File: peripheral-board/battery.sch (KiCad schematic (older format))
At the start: 19 parts

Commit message: added audio jack
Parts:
- U5002, U5003: renamed from U?; footprint (none) -> TO_SOT_Packages_SMD:SOT-23
- gave numbers to parts that had none: 17
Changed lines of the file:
@@
 $EndDescr
 $Comp
-L Battery_Cell BT?
+L Battery_Cell BT5001
 U 1 1 589ABFFA
 P 7000 2800
-F 0 "BT?" H 7118 2896 50  0000 L CNN
+F 0 "BT5001" H 7118 2896 50  0000 L CNN
 F 1 "LiPo" H 7118 2805 50  0000 L CNN
 F 2 "" V -3000 810 50  0001 C CNN
@@
 $EndComp
 $Comp
-L TL431 U?
+L TL431 U5002
 U 1 1 589AC001
 P 5550 2800
-F 0 "U?" H 5677 2853 60  0000 L CNN
+F 0 "U5002" H 5677 2853 60  0000 L CNN
 F 1 "TL431" H 5677 2747 60  0000 L CNN
-F 2 "" H -4350 1000 60  0001 C CNN
+F 2 "TO_SOT_Packages_SMD:SOT-23" H -4350 1000 60  0001 C CNN
 F 3 "" H -4350 1000 60  0001 C CNN
 	1    5550 2800
@@
 $EndComp
 $Comp
-L POT RV?
+L POT RV5001
 U 1 1 589AC008
 P 5000 2800
-F 0 "RV?" H 4930 2846 50  0000 R CNN
+F 0 "RV5001" H 4930 2846 50  0000 R CNN
 F 1 "47k" H 4930 2755 50  0000 R CNN
 F 2 "" H -4200 1800 50  0001 C CNN
@@
 $EndComp
 $Comp
-L R R?
+L R R5002
 U 1 1 589AC00F
 P 5000 2500
-F 0 "R?" H 5070 2546 50  0000 L CNN
+F 0 "R5002" H 5070 2546 50  0000 L CNN
 F 1 "150k" H 5070 2455 50  0000 L CNN
 F 2 "" V -3770 1300 50  0001 C CNN
@@
 $EndComp
 $Comp
-L R R?
+L R R5005
 U 1 1 589AC016
 P 5000 3100
-F 0 "R?" H 5070 3146 50  0000 L CNN
+F 0 "R5005" H 5070 3146 50  0000 L CNN
 F 1 "220k" H 5070 3055 50  0000 L CNN
 F 2 "" V -3720 650 50  0001 C CNN
@@
 $EndComp
 $Comp
-L R R?
+L R R5001
 U 1 1 589AC01D
 P 5550 2300
-F 0 "R?" H 5620 2346 50  0000 L CNN
+F 0 "R5001" H 5620 2346 50  0000 L CNN
 F 1 "10k" H 5620 2255 50  0000 L CNN
 F 2 "" V -3720 1100 50  0001 C CNN
@@
 $EndComp
 $Comp
-L R R?
+L R R5003
 U 1 1 589AC024
 P 6100 2900
-F 0 "R?" H 6170 2946 50  0000 L CNN
+F 0 "R5003" H 6170 2946 50  0000 L CNN
 F 1 "40R" H 6170 2855 50  0000 L CNN
 F 2 "" V -3870 800 50  0001 C CNN
@@
 Connection ~ 5550 3300
 $Comp
-L Battery_Cell BT?
+L Battery_Cell BT5002
 U 1 1 589AC03D
 P 7000 3950
-F 0 "BT?" H 7118 4046 50  0000 L CNN
+F 0 "BT5002" H 7118 4046 50  0000 L CNN
 F 1 "LiPo" H 7118 3955 50  0000 L CNN
 F 2 "" V -3000 1960 50  0001 C CNN
@@
 $EndComp
 $Comp
-L TL431 U?
+L TL431 U5003
 U 1 1 589AC044
 P 5550 3950
-F 0 "U?" H 5677 4003 60  0000 L CNN
+F 0 "U5003" H 5677 4003 60  0000 L CNN
 F 1 "TL431" H 5677 3897 60  0000 L CNN
-F 2 "" H -4350 2150 60  0001 C CNN
+F 2 "TO_SOT_Packages_SMD:SOT-23" H -4350 2150 60  0001 C CNN
 F 3 "" H -4350 2150 60  0001 C CNN
 	1    5550 3950
@@
 $EndComp
 $Comp
-L POT RV?
+L POT RV5002
 U 1 1 589AC04B
 P 5000 3950
-F 0 "RV?" H 4930 3996 50  0000 R CNN
+F 0 "RV5002" H 4930 3996 50  0000 R CNN
 F 1 "47k" H 4930 3905 50  0000 R CNN
 F 2 "" H -4200 2950 50  0001 C CNN
@@
 $EndComp
 $Comp
-L R R?
+L R R5007
 U 1 1 589AC052
 P 5000 3650
-F 0 "R?" H 5070 3696 50  0000 L CNN
+F 0 "R5007" H 5070 3696 50  0000 L CNN
 F 1 "150k" H 5070 3605 50  0000 L CNN
 F 2 "" V -3770 2450 50  0001 C CNN
@@
 $EndComp
 $Comp
-L R R?
+L R R5010
 U 1 1 589AC059
 P 5000 4250
-F 0 "R?" H 5070 4296 50  0000 L CNN
+F 0 "R5010" H 5070 4296 50  0000 L CNN
 F 1 "220k" H 5070 4205 50  0000 L CNN
 F 2 "" V -3720 1800 50  0001 C CNN
@@
 $EndComp
 $Comp
-L R R?
+L R R5006
 U 1 1 589AC060
 P 5550 3450
-F 0 "R?" H 5620 3496 50  0000 L CNN
+F 0 "R5006" H 5620 3496 50  0000 L CNN
 F 1 "10k" H 5620 3405 50  0000 L CNN
 F 2 "" V -3720 2250 50  0001 C CNN
@@
 $EndComp
 $Comp
-L R R?
+L R R5008
 U 1 1 589AC067
 P 6100 4050
-F 0 "R?" H 6170 4096 50  0000 L CNN
+F 0 "R5008" H 6170 4096 50  0000 L CNN
 F 1 "40R" H 6170 4005 50  0000 L CNN
 F 2 "" V -3870 1950 50  0001 C CNN
@@
 Connection ~ 5550 4450
 $Comp
-L Thermistor_NTC TH?
+L Thermistor_NTC TH5001
 U 1 1 589AC07A
 P 4150 4250
-F 0 "TH?" H 4247 4296 50  0000 L CNN
+F 0 "TH5001" H 4247 4296 50  0000 L CNN
 F 1 "10k" H 4247 4205 50  0000 L CNN
 F 2 "" H -3550 3150 50  0001 C CNN
@@
 $EndComp
 $Comp
-L Q_PMOS_DGS Q?
+L Q_PMOS_DGS Q5001
 U 1 1 589AC081
 P 6000 2500
-F 0 "Q?" H 6206 2454 50  0000 L CNN
+F 0 "Q5001" H 6206 2454 50  0000 L CNN
 F 1 "Q_PMOS_DGS" H 6206 2545 50  0000 L CNN
 F 2 "" H -3400 1600 50  0001 C CNN
@@
 $EndComp
 $Comp
-L Q_PMOS_DGS Q?
+L Q_PMOS_DGS Q5002
 U 1 1 589AC088
 P 6000 3650
-F 0 "Q?" H 6206 3604 50  0000 L CNN
+F 0 "Q5002" H 6206 3604 50  0000 L CNN
 F 1 "Q_PMOS_DGS" H 6206 3695 50  0000 L CNN
 F 2 "" H -3400 2750 50  0001 C CNN
@@
 Connection ~ 7000 3300
 $Comp
-L R R?
+L R R5004
 U 1 1 589AEB2B
 P 6400 2900
-F 0 "R?" H 6470 2946 50  0000 L CNN
+F 0 "R5004" H 6470 2946 50  0000 L CNN
 F 1 "40R" H 6470 2855 50  0000 L CNN
 F 2 "" V -3570 800 50  0001 C CNN
@@
 	6400 3050 6100 3050
 $Comp
-L R R?
+L R R5009
 U 1 1 589AEC5C
 P 6400 4050
-F 0 "R?" H 6470 4096 50  0000 L CNN
+F 0 "R5009" H 6470 4096 50  0000 L CNN
 F 1 "40R" H 6470 4005 50  0000 L CNN
 F 2 "" V -3570 1950 50  0001 C CNN

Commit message: audio circuitry
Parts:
- R5001, R5002, R5003, R5004, R5005, R5006, R5007, R5008, R5009, R5010: footprint (none) -> Resistors_SMD:R_0805
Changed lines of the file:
@@
 EESchema Schematic File Version 2
+LIBS:peripheral-board-rescue
 LIBS:power
 LIBS:device
@@
 LIBS:digital-pot
 LIBS:vref
+LIBS:switches
 LIBS:peripheral-board-cache
 EELAYER 26 0
@@
 F 0 "R5002" H 5070 2546 50  0000 L CNN
 F 1 "150k" H 5070 2455 50  0000 L CNN
-F 2 "" V -3770 1300 50  0001 C CNN
+F 2 "Resistors_SMD:R_0805" V -3770 1300 50  0001 C CNN
 F 3 "" H -3700 1300 50  0001 C CNN
 	1    5000 2500
@@
 F 0 "R5005" H 5070 3146 50  0000 L CNN
 F 1 "220k" H 5070 3055 50  0000 L CNN
-F 2 "" V -3720 650 50  0001 C CNN
+F 2 "Resistors_SMD:R_0805" V -3720 650 50  0001 C CNN
 F 3 "" H -3650 650 50  0001 C CNN
 	1    5000 3100
@@
 F 0 "R5001" H 5620 2346 50  0000 L CNN
 F 1 "10k" H 5620 2255 50  0000 L CNN
-F 2 "" V -3720 1100 50  0001 C CNN
+F 2 "Resistors_SMD:R_0805" V -3720 1100 50  0001 C CNN
 F 3 "" H -3650 1100 50  0001 C CNN
 	1    5550 2300
@@
 F 0 "R5003" H 6170 2946 50  0000 L CNN
 F 1 "40R" H 6170 2855 50  0000 L CNN
-F 2 "" V -3870 800 50  0001 C CNN
+F 2 "Resistors_SMD:R_0805" V -3870 800 50  0001 C CNN
 F 3 "" H -3800 800 50  0001 C CNN
 	1    6100 2900
@@
 F 0 "R5007" H 5070 3696 50  0000 L CNN
 F 1 "150k" H 5070 3605 50  0000 L CNN
-F 2 "" V -3770 2450 50  0001 C CNN
+F 2 "Resistors_SMD:R_0805" V -3770 2450 50  0001 C CNN
 F 3 "" H -3700 2450 50  0001 C CNN
 	1    5000 3650
@@
 F 0 "R5010" H 5070 4296 50  0000 L CNN
 F 1 "220k" H 5070 4205 50  0000 L CNN
-F 2 "" V -3720 1800 50  0001 C CNN
+F 2 "Resistors_SMD:R_0805" V -3720 1800 50  0001 C CNN
 F 3 "" H -3650 1800 50  0001 C CNN
 	1    5000 4250
@@
 F 0 "R5006" H 5620 3496 50  0000 L CNN
 F 1 "10k" H 5620 3405 50  0000 L CNN
-F 2 "" V -3720 2250 50  0001 C CNN
+F 2 "Resistors_SMD:R_0805" V -3720 2250 50  0001 C CNN
 F 3 "" H -3650 2250 50  0001 C CNN
 	1    5550 3450
@@
 F 0 "R5008" H 6170 4096 50  0000 L CNN
 F 1 "40R" H 6170 4005 50  0000 L CNN
-F 2 "" V -3870 1950 50  0001 C CNN
+F 2 "Resistors_SMD:R_0805" V -3870 1950 50  0001 C CNN
 F 3 "" H -3800 1950 50  0001 C CNN
 	1    6100 4050
@@
 F 0 "R5004" H 6470 2946 50  0000 L CNN
 F 1 "40R" H 6470 2855 50  0000 L CNN
-F 2 "" V -3570 800 50  0001 C CNN
+F 2 "Resistors_SMD:R_0805" V -3570 800 50  0001 C CNN
 F 3 "" H -3500 800 50  0001 C CNN
 	1    6400 2900
@@
 F 0 "R5009" H 6470 4096 50  0000 L CNN
 F 1 "40R" H 6470 4005 50  0000 L CNN
-F 2 "" V -3570 1950 50  0001 C CNN
+F 2 "Resistors_SMD:R_0805" V -3570 1950 50  0001 C CNN
 F 3 "" H -3500 1950 50  0001 C CNN
 	1    6400 4050

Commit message: power supply component placement
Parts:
- removed Q5001, Q5002: Q_PMOS_DGS, symbol Q_PMOS_DGS
- added Q5001, Q5002: IRLML2244TRPbF, TO_SOT_Packages_SMD:SOT-23, symbol Q_PMOS_GSD
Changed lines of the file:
@@
 	1    0    0    -1
-$EndComp
-$Comp
-L Q_PMOS_DGS Q5001
-U 1 1 589AC081
-P 6000 2500
-F 0 "Q5001" H 6206 2454 50  0000 L CNN
-F 1 "Q_PMOS_DGS" H 6206 2545 50  0000 L CNN
-F 2 "" H -3400 1600 50  0001 C CNN
-F 3 "" H -3600 1500 50  0001 C CNN
-	1    6000 2500
-	1    0    0    1
-$EndComp
-$Comp
-L Q_PMOS_DGS Q5002
-U 1 1 589AC088
-P 6000 3650
-F 0 "Q5002" H 6206 3604 50  0000 L CNN
-F 1 "Q_PMOS_DGS" H 6206 3695 50  0000 L CNN
-F 2 "" H -3400 2750 50  0001 C CNN
-F 3 "" H -3600 2650 50  0001 C CNN
-	1    6000 3650
-	1    0    0    1
 $EndComp
 Text HLabel 3350 2150 0    60   UnSpc ~ 0
@@
 Text Notes 6150 4300 0    60   ~ 0
 2 × 1/4 W
+$Comp
+L Q_PMOS_GSD Q5001
+U 1 1 58A97AA9
+P 6000 2500
+F 0 "Q5001" H 6206 2454 50  0000 L CNN
+F 1 "IRLML2244TRPbF" H 6206 2545 50  0000 L CNN
+F 2 "TO_SOT_Packages_SMD:SOT-23" H -850 700 50  0001 C CNN
+F 3 "" H -1050 600 50  0001 C CNN
+	1    6000 2500
+	1    0    0    1
+$EndComp
+$Comp
+L Q_PMOS_GSD Q5002
+U 1 1 58A97BDE
+P 6000 3650
+F 0 "Q5002" H 6206 3604 50  0000 L CNN
+F 1 "IRLML2244TRPbF" H 6206 3695 50  0000 L CNN
+F 2 "TO_SOT_Packages_SMD:SOT-23" H -850 1850 50  0001 C CNN
+F 3 "" H -1050 1750 50  0001 C CNN
+	1    6000 3650
+	1    0    0    1
+$EndComp
 $EndSCHEMATC

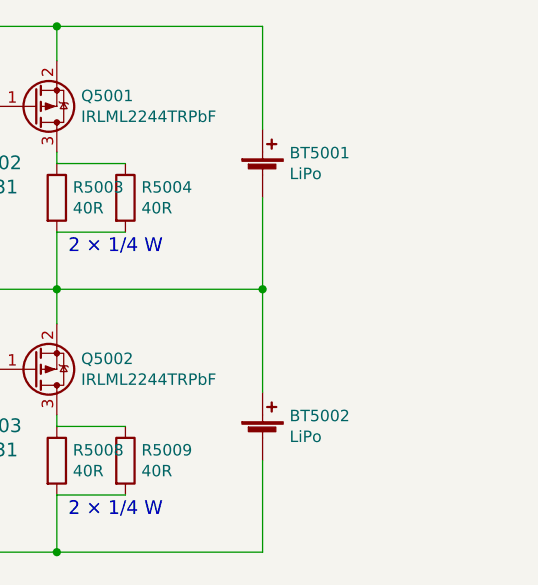
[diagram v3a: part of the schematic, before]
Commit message: audio components placement
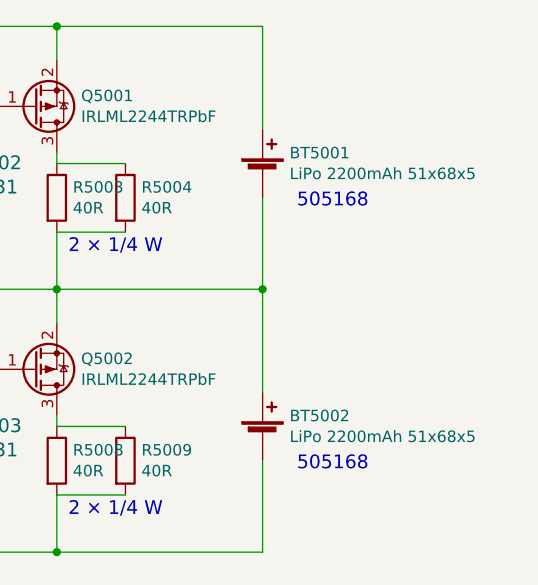
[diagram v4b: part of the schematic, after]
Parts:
- BT5001, BT5002: value LiPo -> LiPo 2200mAh 51x68x5
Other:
- note added: "505168"
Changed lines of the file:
@@
 P 7000 2800
 F 0 "BT5001" H 7118 2896 50  0000 L CNN
-F 1 "LiPo" H 7118 2805 50  0000 L CNN
+F 1 "LiPo 2200mAh 51x68x5" H 7118 2805 50  0000 L CNN
 F 2 "" V -3000 810 50  0001 C CNN
 F 3 "" V -3000 810 50  0001 C CNN
@@
 P 7000 3950
 F 0 "BT5002" H 7118 4046 50  0000 L CNN
-F 1 "LiPo" H 7118 3955 50  0000 L CNN
+F 1 "LiPo 2200mAh 51x68x5" H 7118 3955 50  0000 L CNN
 F 2 "" V -3000 1960 50  0001 C CNN
 F 3 "" V -3000 1960 50  0001 C CNN
@@
 	1    0    0    1
 $EndComp
+Text Notes 7150 2950 0    60   ~ 0
+505168
+Text Notes 7150 4100 0    60   ~ 0
+505168
 $EndSCHEMATC

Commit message: routed traces.
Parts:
- TH5001: footprint (none) -> Capacitors_ThroughHole:CP_Radial_Tantal_D4.5mm_P2.50mm
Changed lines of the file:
@@
 F 0 "TH5001" H 4247 4296 50  0000 L CNN
 F 1 "10k" H 4247 4205 50  0000 L CNN
-F 2 "" H -3550 3150 50  0001 C CNN
+F 2 "Capacitors_ThroughHole:CP_Radial_Tantal_D4.5mm_P2.50mm" H -3550 3150 50  0001 C CNN
 F 3 "" H -3550 3150 50  0001 C CNN
 	1    4150 4250

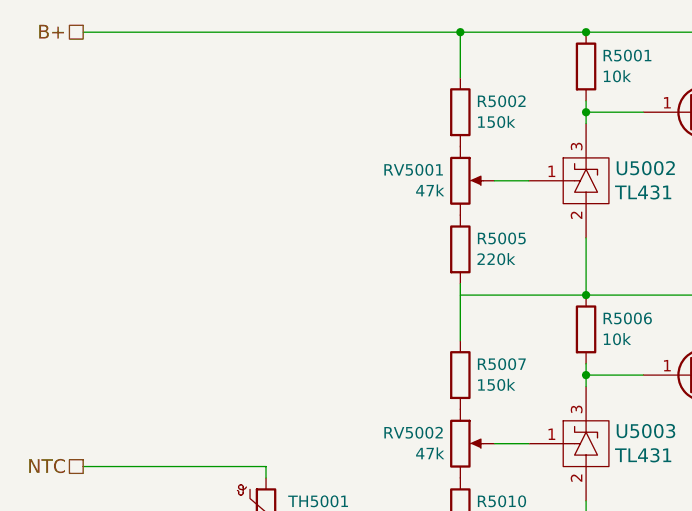
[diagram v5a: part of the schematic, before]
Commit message: misc traces, headphone jack 3d
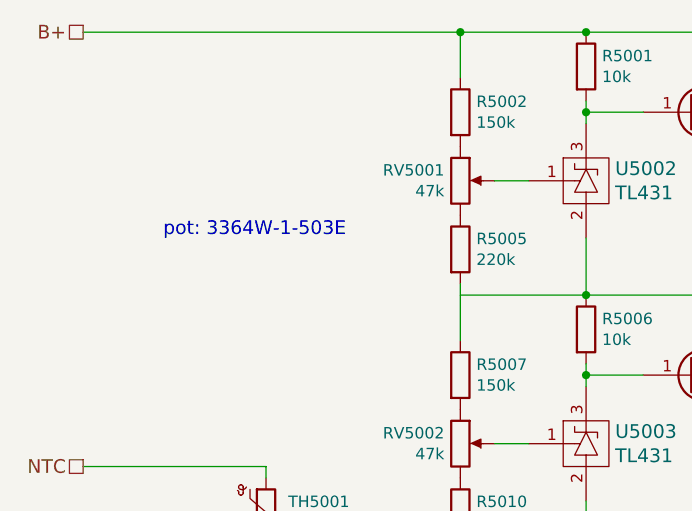
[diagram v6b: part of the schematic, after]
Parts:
- RV5001, RV5002: footprint (none) -> lib:3364W
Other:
- note added: "pot: 3364W-1-503E"
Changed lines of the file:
@@
 F 0 "RV5001" H 4930 2846 50  0000 R CNN
 F 1 "47k" H 4930 2755 50  0000 R CNN
-F 2 "" H -4200 1800 50  0001 C CNN
+F 2 "lib:3364W" H -4200 1800 50  0001 C CNN
 F 3 "" H -4200 1800 50  0001 C CNN
 	1    5000 2800
@@
 F 0 "RV5002" H 4930 3996 50  0000 R CNN
 F 1 "47k" H 4930 3905 50  0000 R CNN
-F 2 "" H -4200 2950 50  0001 C CNN
+F 2 "lib:3364W" H -4200 2950 50  0001 C CNN
 F 3 "" H -4200 2950 50  0001 C CNN
 	1    5000 3950
@@
 Text Notes 7150 4100 0    60   ~ 0
 505168
+Text Notes 3700 3050 0    60   ~ 0
+pot: 3364W-1-503E
 $EndSCHEMATC

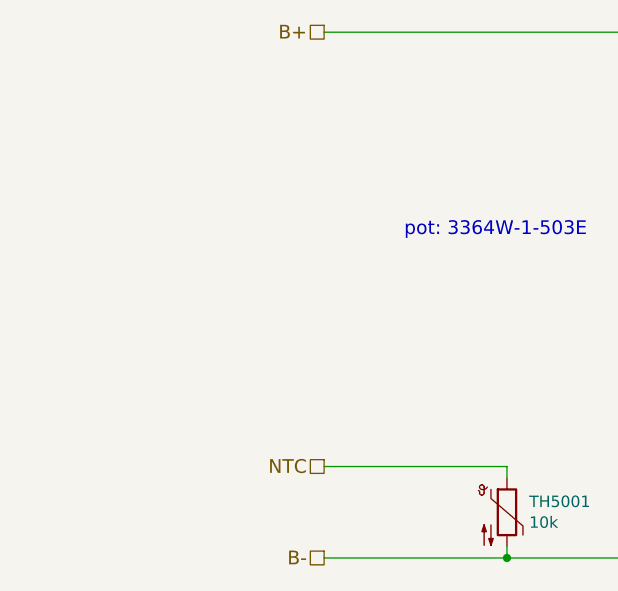
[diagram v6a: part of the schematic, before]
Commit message: added display board
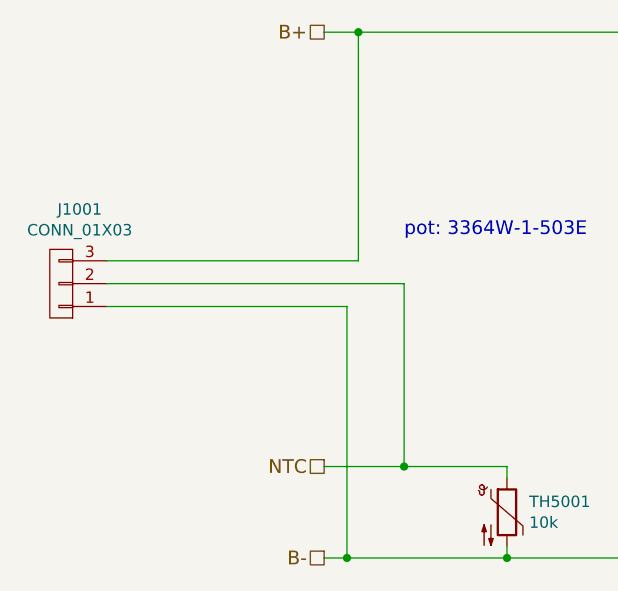
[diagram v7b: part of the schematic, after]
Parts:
- added J1001: CONN_01X03, Socket_Strips:Socket_Strip_Straight_1x03_Pitch2.54mm, symbol CONN_01X03
- BT5001, BT5002: footprint (none) -> Socket_Strips:Socket_Strip_Straight_1x02_Pitch1.27mm
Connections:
- net B+: now also J1001.3 (P3)
- net B-: now also J1001.1 (P1)
- net NTC: now also J1001.2 (P2)
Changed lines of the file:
@@
 EESchema Schematic File Version 2
-LIBS:peripheral-board-rescue
 LIBS:power
 LIBS:device
@@
 LIBS:contrib
 LIBS:valves
-LIBS:amp
-LIBS:card-edge
-LIBS:switchmode
-LIBS:joystick
-LIBS:digital-pot
 LIBS:vref
-LIBS:switches
-LIBS:peripheral-board-cache
+LIBS:battery-cache
 EELAYER 26 0
 EELAYER END
 $Descr A4 11693 8268
 encoding utf-8
-Sheet 5 10
+Sheet 1 1
 Title ""
 Date ""
@@
 F 0 "BT5001" H 7118 2896 50  0000 L CNN
 F 1 "LiPo 2200mAh 51x68x5" H 7118 2805 50  0000 L CNN
-F 2 "" V -3000 810 50  0001 C CNN
+F 2 "Socket_Strips:Socket_Strip_Straight_1x02_Pitch1.27mm" V -3000 810 50  0001 C CNN
 F 3 "" V -3000 810 50  0001 C CNN
 	1    7000 2800
@@
 F 0 "BT5002" H 7118 4046 50  0000 L CNN
 F 1 "LiPo 2200mAh 51x68x5" H 7118 3955 50  0000 L CNN
-F 2 "" V -3000 1960 50  0001 C CNN
+F 2 "Socket_Strips:Socket_Strip_Straight_1x02_Pitch1.27mm" V -3000 1960 50  0001 C CNN
 F 3 "" V -3000 1960 50  0001 C CNN
 	1    7000 3950
@@
 Text Notes 3700 3050 0    60   ~ 0
 pot: 3364W-1-503E
+$Comp
+L CONN_01X03 J1001
+U 1 1 58E61493
+P 2200 3250
+F 0 "J1001" H 2119 2925 50  0000 C CNN
+F 1 "CONN_01X03" H 2119 3016 50  0000 C CNN
+F 2 "Socket_Strips:Socket_Strip_Straight_1x03_Pitch2.54mm" H 2200 3250 50  0001 C CNN
+F 3 "" H 2200 3250 50  0001 C CNN
+	1    2200 3250
+	-1   0    0    1
+$EndComp
+Wire Wire Line
+	2400 3150 3500 3150
+Wire Wire Line
+	3500 3150 3500 2150
+Connection ~ 3500 2150
+Wire Wire Line
+	2400 3250 3700 3250
+Wire Wire Line
+	3700 3250 3700 4050
+Connection ~ 3700 4050
+Wire Wire Line
+	2400 3350 3450 3350
+Wire Wire Line
+	3450 3350 3450 4450
+Connection ~ 3450 4450
 $EndSCHEMATC

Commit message: fixed faulty schematic in battery balancer
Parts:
- U5002, U5003: symbol TL431 -> TL431DBZ
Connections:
- net B-: now also U5003.3 (A); no longer U5003.2
- net at BT5001.2 (-), BT5002.1 (+), Q5002.2 (S)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: now also R5005.2, R5007.1, U5002.3 (A); no longer U5002.2
- net at U5002.1 (K): now also Q5001.1 (G), R5001.2; no longer RV5001.2
- net at U5003.1 (K): now also Q5002.1 (G), R5006.2; no longer RV5002.2
- new net: RV5001.2, U5002.2 (REF)
- new net: RV5002.2, U5003.2 (REF)
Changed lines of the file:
@@
 LIBS:valves
 LIBS:vref
+LIBS:references
 LIBS:battery-cache
 EELAYER 26 0
@@
 $EndComp
 $Comp
-L TL431 U5002
+L TL431DBZ U5002
 U 1 1 589AC001
 P 5550 2800
-F 0 "U5002" H 5677 2853 60  0000 L CNN
-F 1 "TL431" H 5677 2747 60  0000 L CNN
+F 0 "U5002" V 5600 2450 60  0000 L CNN
+F 1 "TL431" V 5400 2450 60  0000 L CNN
 F 2 "TO_SOT_Packages_SMD:SOT-23" H -4350 1000 60  0001 C CNN
 F 3 "" H -4350 1000 60  0001 C CNN
 	1    5550 2800
-	1    0    0    -1
+	0    -1   -1   0
 $EndComp
 $Comp
@@
 	5800 2500 5550 2500
 Wire Wire Line
-	5550 2450 5550 2550
+	5550 2450 5550 2700
 Connection ~ 5550 2500
 Wire Wire Line
-	5300 2800 5150 2800
-Wire Wire Line
-	5550 3050 5550 3300
+	5150 2800 5450 2800
+Wire Wire Line
+	5550 2900 5550 3300
 Connection ~ 5550 3300
 $Comp
@@
 $EndComp
 $Comp
-L TL431 U5003
+L TL431DBZ U5003
 U 1 1 589AC044
 P 5550 3950
-F 0 "U5003" H 5677 4003 60  0000 L CNN
-F 1 "TL431" H 5677 3897 60  0000 L CNN
+F 0 "U5003" V 5600 3600 60  0000 L CNN
+F 1 "TL431" V 5400 3600 60  0000 L CNN
 F 2 "TO_SOT_Packages_SMD:SOT-23" H -4350 2150 60  0001 C CNN
 F 3 "" H -4350 2150 60  0001 C CNN
 	1    5550 3950
-	1    0    0    -1
+	0    -1   -1   0
 $EndComp
 $Comp
@@
 	5800 3650 5550 3650
 Wire Wire Line
-	5550 3600 5550 3700
+	5550 3600 5550 3850
 Connection ~ 5550 3650
 Wire Wire Line
-	5300 3950 5150 3950
-Wire Wire Line
-	5550 4200 5550 4450
+	5150 3950 5450 3950
+Wire Wire Line
+	5550 4050 5550 4450
 Connection ~ 5550 4450
 $Comp
@@
 	3450 3350 3450 4450
 Connection ~ 3450 4450
+Connection ~ 5000 3300
 $EndSCHEMATC
